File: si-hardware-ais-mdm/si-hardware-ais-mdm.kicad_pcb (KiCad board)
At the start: 4 copper layers, 78.2 x 30 mm, 96 parts, among them J1 CN1, J2 CN2, J3 Conn_Coaxial, J4 USB_C_Receptacle_USB2.0_16P, Q1 IRLML6401, SW1 SW_Push, SW2 SW_Push, U1 LMR14206, U2 MCP73811T-420I-OT, U3 Si4362, U4 TA0395A, U5 Si4362, U6 ESP32-C6-MINI-1-H4, U7 LIS331HH, U9 24AA02E-OT, Y1 30MHz, Y2 30MHz

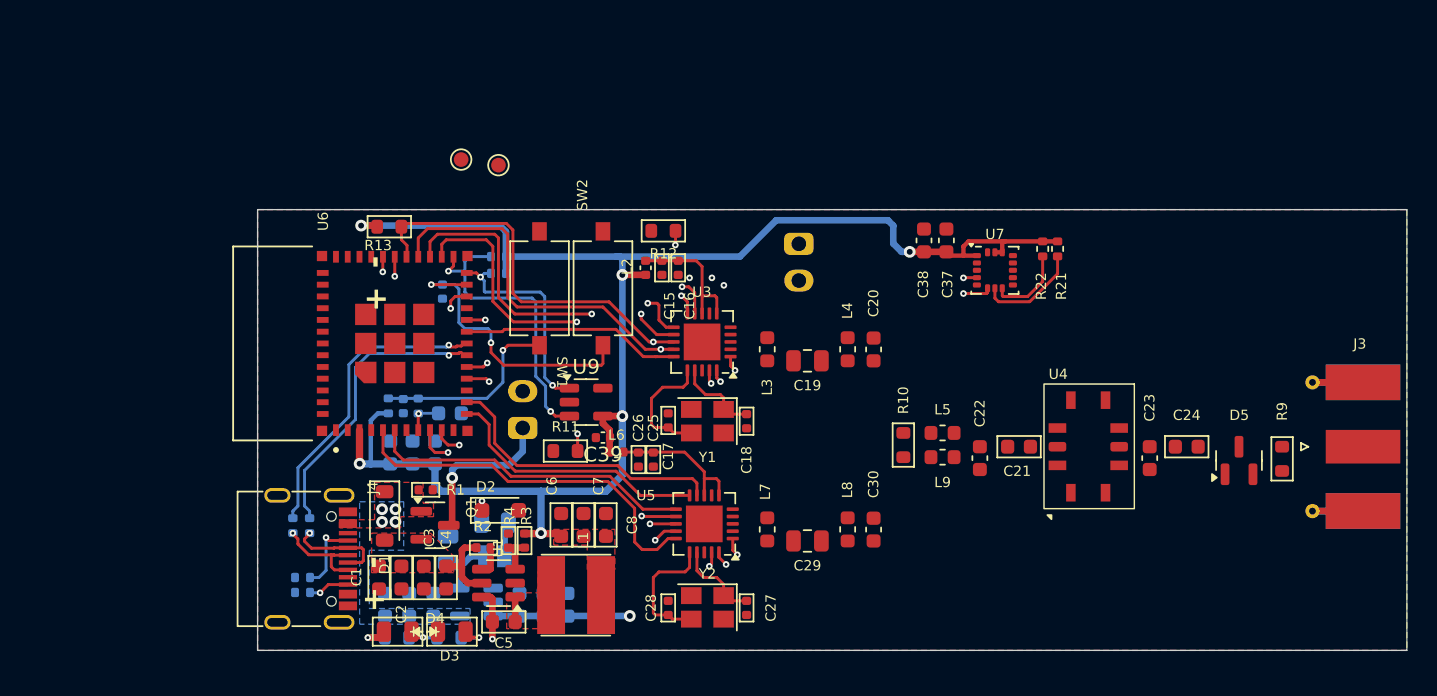
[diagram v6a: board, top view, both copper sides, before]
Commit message: added ic charger
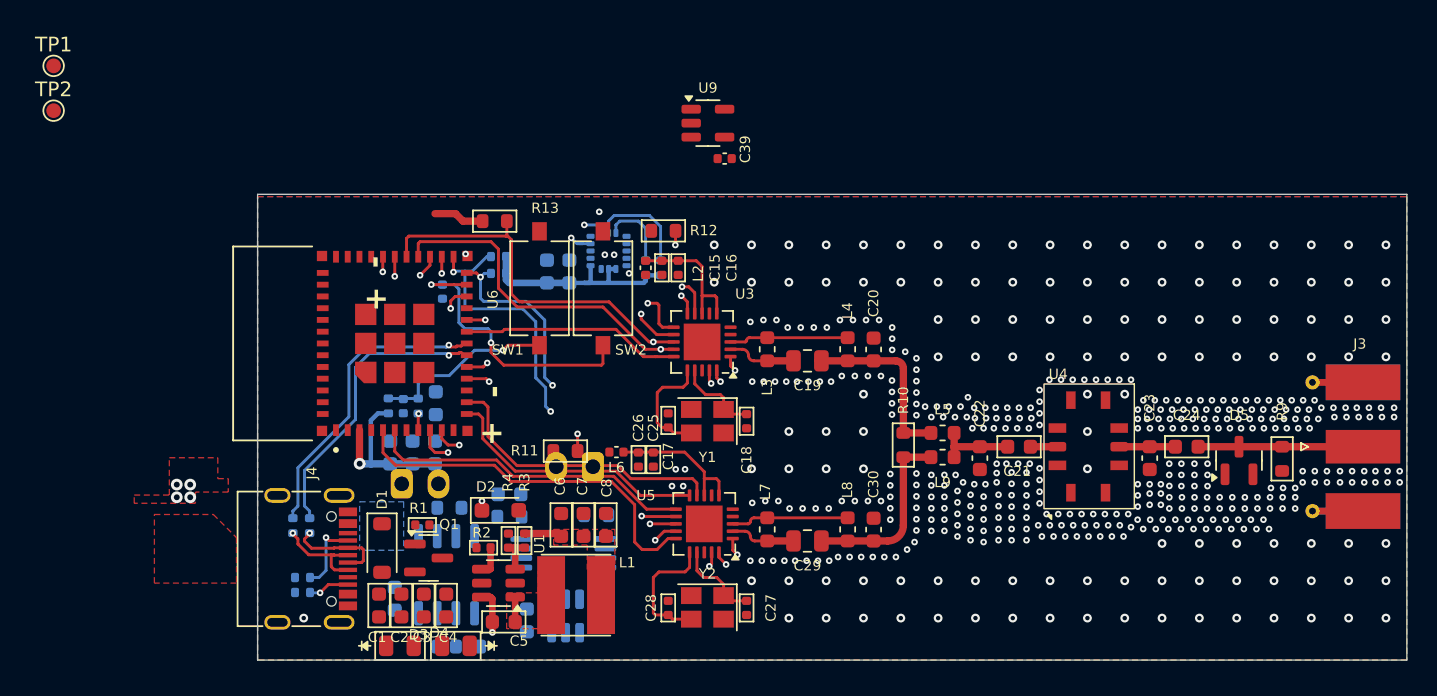
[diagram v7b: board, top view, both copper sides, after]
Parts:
- removed C10, C13: 1uF/10V, CTS_Capacitor_SMD:C_0603_1608Metric
- removed C9: 10uF/6V, CTS_Capacitor_SMD:C_0603_1608Metric
- removed JP1: SolderJumper_2_Open, Jumper:SolderJumper-2_P1.3mm_Open_Pad1.0x1.5mm
- removed R7, R8: 2K, CTS_Resistor_SMD:R_0805_2012Metric
- removed U2: MCP73811T-420I-OT, Package_TO_SOT_SMD:SOT-23-5
- added R24: 1.2K, CTS_Resistor_SMD:R_0603_1608Metric, B.Cu at (134.1, 103.6)
- added R25: 1K, CTS_Resistor_SMD:R_0603_1608Metric, B.Cu at (144.1, 104.1)
- added R26: 100R, CTS_Resistor_SMD:R_0603_1608Metric, B.Cu at (138.2, 104.2)
- added U11: FS8205, Package_SO:TSSOP-8_4.4x3mm_P0.65mm, B.Cu at (141.8, 106.7)
- added U12: DW01A, Package_TO_SOT_SMD:SOT-23-6, B.Cu at (142.0, 110.9)
- added U8: TP4056, Package_SO:SOP-8_3.9x4.9mm_P1.27mm, B.Cu at (133.9, 108.1)
- C37, C38, R21, R22, U7: moved to B.Cu
- J2: value CN2 -> CN1
- R5, R6: value 10K -> 1K
- moved TP1 31.0 mm to (107.1, 73.5)
- moved TP2 27.9 mm to (107.1, 76.6)
- moved C37 27.3 mm to (140.7, 87.5)
- moved R22 27.1 mm to (147.4, 87.3), turned to 90 degrees
- moved R21 27.1 mm to (148.4, 87.3), turned to 90 degrees
- moved U7 26.3 mm to (144.9, 86.1)
- moved C38 24.2 mm to (142.2, 87.5)
- moved C39 20.7 mm to (152.8, 79.8)
- moved U9 20.7 mm to (151.7, 77.4)
- moved J2 20.7 mm to (143.8, 100.8), turned to 180 degrees
- moved J1 9.07 mm to (130.8, 102.0), turned to 0 degrees
- moved C14 8.49 mm to (138.2, 102.7), turned to 180 degrees
- moved R13 7.19 mm to (137.2, 84.1)
- moved R1 2.40 mm to (132.2, 104.7)
- moved Q1 2.27 mm to (132.7, 107.0)
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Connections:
- net /MCU/mdm.SDN1 renamed RX0
- net /MCU/mdm.SDN2 renamed TX0
- net Net-(U6-EN) renamed EN
- C1 pad 2: GND -> bat-
- C11 pad 1: GND -> bat-
- C12 pad 1: GND -> bat-
- C12 pad 2: V_BATT -> Net-(U12-VCC)
- C14 pad 1: GND -> bat+
- C14 pad 2: V_BATT -> bat-
- C15 pad 2: GND -> bat-
- C16 pad 2: GND -> bat-
- C17 pad 2: GND -> bat-
- C18 pad 1: GND -> bat-
- C2 pad 2: GND -> bat-
- C20 pad 1: GND -> bat-
- C22 pad 2: GND -> bat-
- C23 pad 2: GND -> bat-
- C25 pad 2: GND -> bat-
- C26 pad 2: GND -> bat-
- C27 pad 1: GND -> bat-
- C28 pad 2: GND -> bat-
- C3 pad 2: GND -> bat-
- C30 pad 1: GND -> bat-
- C31 pad 2: GND -> bat-
- C32 pad 1: GND -> bat-
- C33 pad 2: GND -> bat-
- C34 pad 1: GND -> bat-
- C35 pad 1: GND -> bat-
- C36 pad 1: GND -> bat-
- C37 pad 1: GND -> bat-
- C38 pad 1: GND -> bat-
- C39 pad 2: GND -> bat-
- C4 pad 2: GND -> bat-
- C6 pad 2: GND -> bat-
- C7 pad 2: GND -> bat-
- C8 pad 2: GND -> bat-
- D2 pad 2: GND -> bat-
- D3 pad 1: GND -> Net-(D3-K)
- D3 pad 2: Net-(D3-A) -> V_BUS
- D4 pad 2: Net-(D4-A) -> V_BUS
- D5 pad 1: GND -> bat-
- D5 pad 2: GND -> bat-
- J1 pad 1: V_BATT -> bat-
- J1 pad 2: GND -> bat+
- J2 pad 1: V_BATT -> bat-
- J2 pad 2: GND -> bat+
- J3 pad 2: GND -> bat-
- J4 pad A1: GND -> bat-
- J4 pad A12: GND -> bat-
- J4 pad B1: GND -> bat-
- J4 pad B12: GND -> bat-
- J4 pad S1: GND -> bat-
- R1 pad 2: GND -> bat-
- R11 pad 2: GND -> bat-
- R12 pad 2: GND -> bat-
- R19 pad 2: GND -> bat-
- R20 pad 2: GND -> bat-
- R4 pad 2: GND -> bat-
- R5 pad 1: Net-(D3-A) -> Net-(D3-K)
- R5 pad 2: Net-(D4-K) -> Net-(U8-STDBY)
- R6 pad 1: V_BUS -> Net-(D4-K)
- R6 pad 2: Net-(D4-A) -> Net-(U8-CHRG)
- R9 pad 2: GND -> bat-
- SW1 pad 1: GND -> bat-
- SW2 pad 1: GND -> bat-
- U1 pad 2: GND -> bat-
- U3 pad 18: GND -> bat-
- U3 pad 21: GND -> bat-
- U4 pad 1: GND -> bat-
- U4 pad 10: GND -> bat-
- U4 pad 3: GND -> bat-
- U4 pad 4: GND -> bat-
- U4 pad 5: GND -> bat-
- U4 pad 6: GND -> bat-
- U4 pad 8: GND -> bat-
- U4 pad 9: GND -> bat-
- U5 pad 18: GND -> bat-
- U5 pad 21: GND -> bat-
- U6 pad 1: GND -> bat-
- U6 pad 11: GND -> bat-
- U6 pad 14: GND -> bat-
- U6 pad 2: GND -> bat-
- U6 pad 36: GND -> bat-
- U6 pad 37: GND -> bat-
- U6 pad 38: GND -> bat-
- U6 pad 39: GND -> bat-
- U6 pad 40: GND -> bat-
- U6 pad 41: GND -> bat-
- U6 pad 42: GND -> bat-
- U6 pad 43: GND -> bat-
- U6 pad 44: GND -> bat-
- U6 pad 45: GND -> bat-
- U6 pad 46: GND -> bat-
- U6 pad 47: GND -> bat-
- U6 pad 48: GND -> bat-
- U6 pad 49_1: GND -> bat-
- U6 pad 49_2: GND -> bat-
- U6 pad 49_3: GND -> bat-
- U6 pad 49_4: GND -> bat-
- U6 pad 49_5: GND -> bat-
- U6 pad 49_6: GND -> bat-
- U6 pad 49_7: GND -> bat-
- U6 pad 49_8: GND -> bat-
- U6 pad 49_9: GND -> bat-
- U6 pad 50: GND -> bat-
- U6 pad 51: GND -> bat-
- U6 pad 52: GND -> bat-
- U6 pad 53: GND -> bat-
- U7 pad 10: GND -> bat-
- U7 pad 12: GND -> bat-
- U7 pad 13: GND -> bat-
- U7 pad 16: GND -> bat-
- U7 pad 5: GND -> bat-
- U9 pad 2: GND -> bat-
- Y1 pad 2: GND -> bat-
- Y1 pad 4: GND -> bat-
- Y2 pad 2: GND -> bat-
- Y2 pad 4: GND -> bat-
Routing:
- net +3.3V: track 109.9 -> 34.9 mm, vias 6 -> 1
- net V_BATT: track 64.3 -> 0.00 mm, vias 2 -> 0
- net Net-(C29-Pad1): track 0.00 -> 12.7 mm
- net Net-(C19-Pad1): track 0.00 -> 12.4 mm
- net SCL: track 35.5 -> 23.3 mm, vias 5 -> 3
- net Net-(J3-In): track 0.00 -> 11.2 mm
- net SDA: track 41.2 -> 31.2 mm, vias 4 -> 3
- net TX0: track 42.5 -> 52.1 mm
- net Net-(U3-RXn): track 0.00 -> 8.12 mm
- net Net-(U5-RXn): track 0.00 -> 8.04 mm
- net RX0: track 35.3 -> 42.4 mm
- net Net-(D1A-K): track 5.52 -> 0.00 mm
- net Net-(C21-Pad2): track 0.00 -> 5.30 mm
- net /MCU/mdm.CTS1: track 24.6 -> 19.9 mm
- net Net-(U3-RXp): track 0.00 -> 4.70 mm
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- added copper zone on B.Cu, net bat-
- added copper zone on F.Cu, net bat-
- added copper zone on In1.Cu, net bat-
- added copper zone on In2.Cu, net bat-
- removed copper zone on B.Cu, net GND
- removed copper zone on F.Cu, net GND
- removed copper zone on In1.Cu, net GND
- removed copper zone on In2.Cu, net GND
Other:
- board size 78.2 x 30 mm -> 78.2 x 31.7 mm

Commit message: routing final
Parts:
- removed TP1, TP2: TestPoint, TestPoint:TestPoint_Pad_D1.0mm
- added J5: Conn_01x03_Socket, Connector_PinHeader_2.54mm:PinHeader_1x03_P2.54mm_Horizontal, F.Cu at (124.5, 83.7)
- moved C39 21.6 mm to (141.7, 98.3)
- moved U9 21.6 mm to (141.0, 96.1)
- moved D2 9.30 mm to (138.3, 113.0)
- moved J1 8.74 mm to (136.6, 95.4), turned to -90 degrees
- moved C12 6.05 mm to (135.6, 106.5), turned to 90 degrees
- moved U11 6.02 mm to (138.7, 111.8), turned to 180 degrees
- moved J2 5.62 mm to (145.3, 95.4), turned to -90 degrees
- moved U12 5.50 mm to (138.7, 106.6), turned to 180 degrees
- moved R15 4.78 mm to (127.2, 95.9)
- moved R16 4.78 mm to (125.2, 95.9)
- moved C31 4.78 mm to (126.2, 96.0)
- moved C32 4.76 mm to (128.5, 95.7)
- moved C34 4.43 mm to (128.7, 100.1)
- moved C35 4.43 mm to (127.2, 100.1)
- moved C36 4.43 mm to (125.6, 100.1)
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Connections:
- net RX0 renamed /MCU/mdm.SDN1
- net TX0 renamed /MCU/mdm.SDN2
- net V_BUS renamed V_USB
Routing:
- net +3.3V: track 34.9 -> 70.4 mm, vias 1 -> 10
- net bat+: track 0.00 -> 28.2 mm
- net V_USB: track 0.00 -> 24.4 mm, vias 4 -> 5
- net Net-(U11-G1): track 0.00 -> 13.8 mm
- net Net-(U11-G2): track 0.00 -> 11.9 mm
- net Net-(D2-K): track 12.9 -> 3.79 mm, vias 2 -> 0
- net Net-(U12-VCC): track 0.00 -> 7.27 mm
- net SDA: track 31.2 -> 37.9 mm
- net Net-(U11-D12-Pad1): track 0.00 -> 5.73 mm
- net Net-(D3-K): track 0.00 -> 5.06 mm, vias 0 -> 1
- net Net-(C31-Pad1): track 12.4 -> 16.9 mm
- net /MCU/mdm.CTS1: track 19.9 -> 24.3 mm
- net /MCU/mdm.CTS2: track 18.3 -> 22.6 mm
- net Net-(U8-CHRG): track 0.00 -> 4.22 mm
- net Net-(U8-STDBY): track 0.00 -> 4.17 mm
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- added copper zone on B.Cu, net +3.3V
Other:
- board text added: "TX"
